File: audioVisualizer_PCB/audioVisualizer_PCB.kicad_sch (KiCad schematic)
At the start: 39 parts, among them J1 USB_C_16P, J2 SWD_DEBUG, J3 SPI_LED_MATRIX, U1 AMS1117-3.3, U7 STM32F401CCUx, Y1 ASE-25MHz

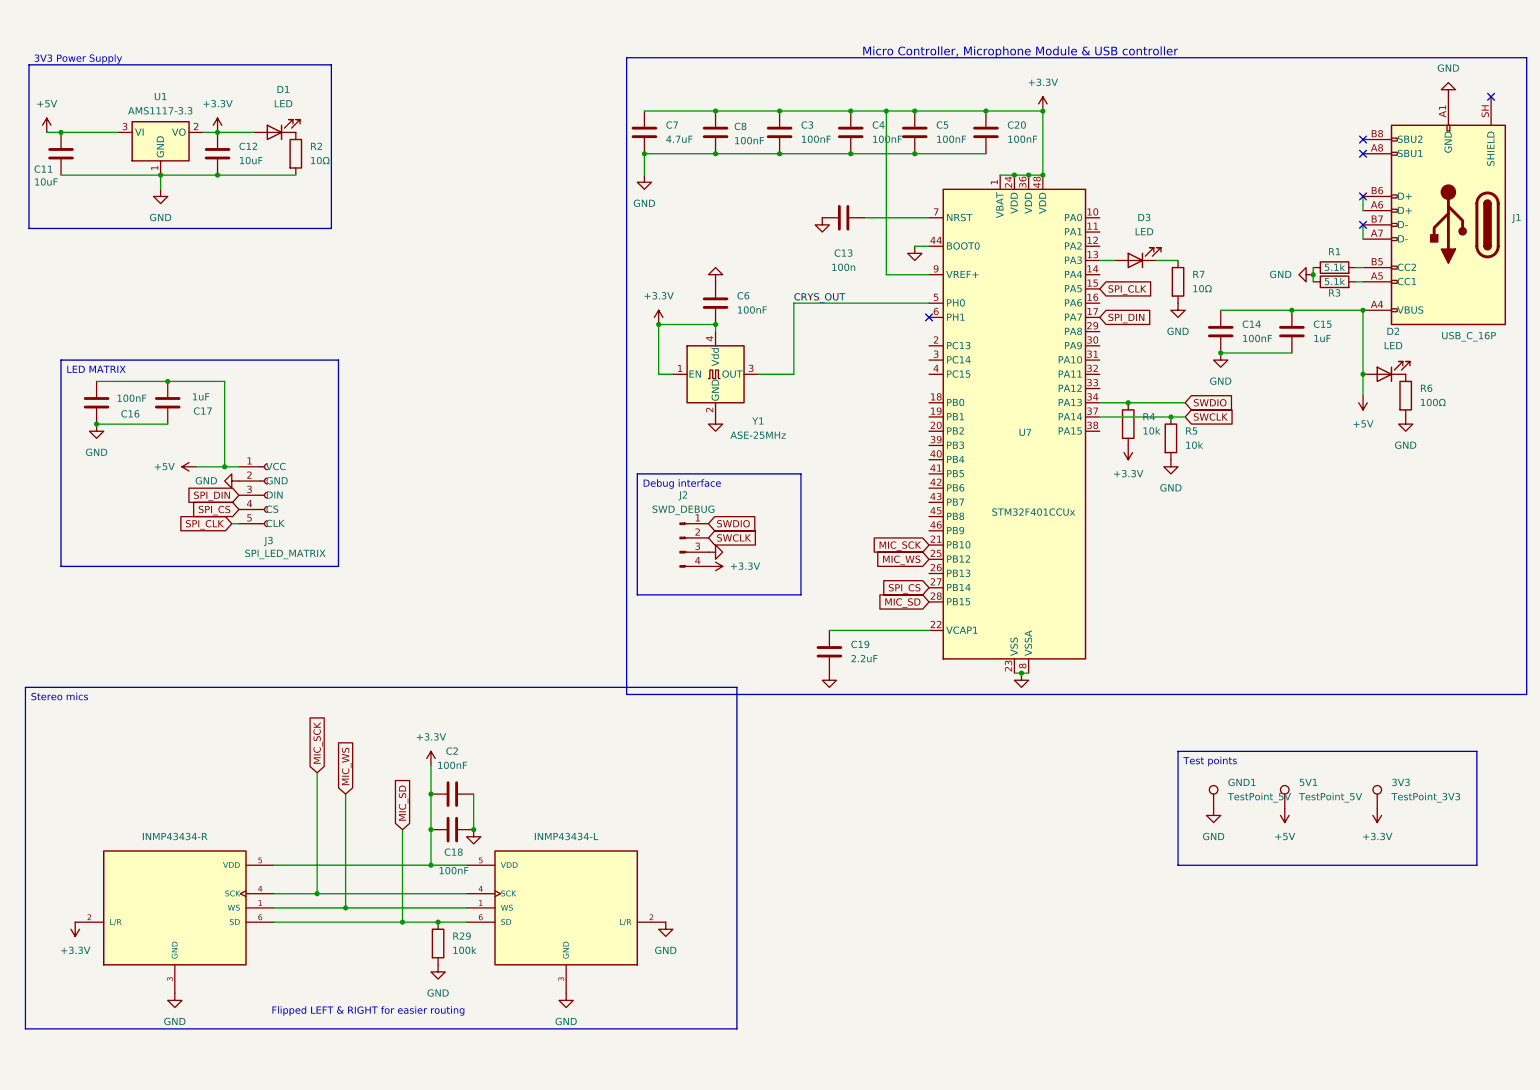
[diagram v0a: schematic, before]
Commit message: update afer review; power fixed?
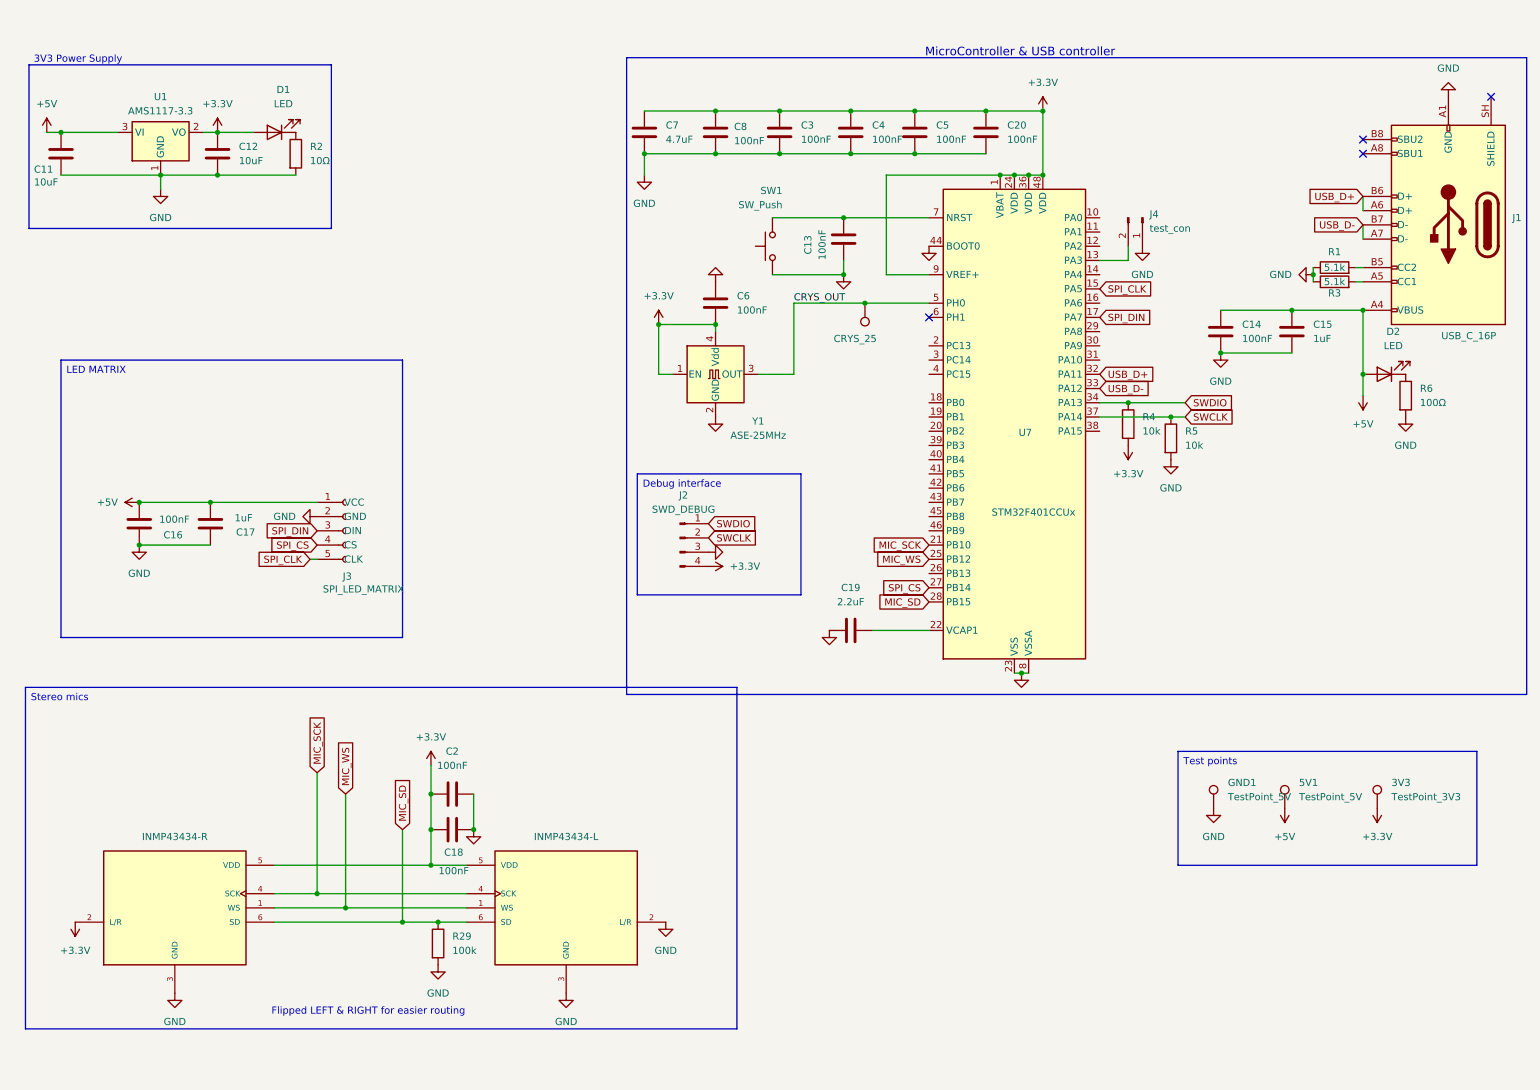
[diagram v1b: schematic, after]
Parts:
- removed D3: LED, LED_SMD:LED_0805_2012Metric, symbol Device:LED
- removed R7: 10Ω, Resistor_SMD:R_0805_2012Metric, symbol Device:R
- added CRYS_25: CRYS_25, TestPoint:TestPoint_Keystone_5015_Micro_Mini, symbol Connector:TestPoint
- added J4: test_con, Connector_PinHeader_2.54mm:PinHeader_1x02_P2.54mm_Vertical, symbol Connector:Conn_01x02_Pin
- added SW1: SW_Push, symbol Switch:SW_Push
- 3V3, 5V1, GND1: footprint TestPoint:TestPoint_Pad_1.0x1.0mm -> TestPoint:TestPoint_Keystone_5015_Micro_Mini
- C13: value 100n -> 100nF
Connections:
- net CRYS_OUT: now also CRYS_25.1
- net GND: now also J4.1 (Pin_1), SW1.1
- net at U7.13 (PA3): now also J4.2 (Pin_2)
- net USB_D+: now reaches U7.32 (PA11)
- net USB_D+: now also J1.A6 (D+), J1.B6 (D+)
- net USB_D-: now reaches U7.33 (PA12)
- net USB_D-: now also J1.A7 (D-), J1.B7 (D-)
- net at C13.1, U7.7 (NRST): now also SW1.2
- no-connect marks 6 -> 4
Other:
- note added: "MicroController & USB controller"
- note removed: "Micro Controller, Microphone Module & USB controller"
- moved on the sheet: C13, C16, C17, C19, J3

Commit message: update
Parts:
- removed J4: test_con, Connector_PinHeader_2.54mm:PinHeader_1x02_P2.54mm_Vertical, symbol Connector:Conn_01x02_Pin
- removed U7: STM32F401CCUx, Package_DFN_QFN:QFN-48-1EP_7x7mm_P0.5mm_EP5.6x5.6mm, symbol MCU_ST_STM32F4:STM32F401CCUx
- added R7: 10kΩ, Resistor_SMD:R_0805_2012Metric, symbol Device:R
- added U2: STM32F401RETx, Package_QFP:LQFP-64_10x10mm_P0.5mm, symbol MCU_ST_STM32F4:STM32F401RETx
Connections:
- net +3.3V: now also R7.1, U2.1 (VBAT), U2.19 (VDD), U2.32 (VDD), U2.48 (VDD), U2.64 (VDD)
- net CRYS_OUT: now also U2.5 (PH0)
- net GND: now also U2.12 (VSSA), U2.18 (VSS), U2.31 (VSS), U2.47 (VSS), U2.60 (BOOT0), U2.63 (VSS)
- net MIC_SCK: now also U2.51 (PC10)
- net MIC_SD: now also U2.53 (PC12)
- net MIC_WS: now also U2.50 (PA15)
- net SPI_CLK: now also U2.34 (PB13)
- net SPI_CS: now also U2.35 (PB14)
- net SPI_DIN: now also U2.36 (PB15)
- net SWCLK: now also U2.49 (PA14)
- net SWDIO: now also U2.46 (PA13)
- net at C19.1: now also U2.30 (VCAP1)
- net at C13.1, SW1.2: now also R7.2, U2.7 (NRST)
- no-connect marks 4 -> 3
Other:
- moved on the sheet: C13, C14, C15, C18, C19, C2, D2, J1, R1, R29, R3, R4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

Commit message: new mcu
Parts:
- removed R7: 10kΩ, Resistor_SMD:R_0805_2012Metric, symbol Device:R
- added R8: 10k, Resistor_SMD:R_0805_2012Metric, symbol Device:R_Small
- SW1: footprint (none) -> Button_Switch_SMD:SW_SPST_TS-1088-xR020
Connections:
- net +3.3V: now also R8.1
- net at C13.1, SW1.2, U2.7 (NRST): now also R8.2
- no-connect marks 3 -> 4
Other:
- moved on the sheet: C13, C14, C15, D2, J1, R1, R3, R6, SW1

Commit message: updated workflow and removed production folder
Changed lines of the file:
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@@
 	)
 	(rectangle
+		(start 17.78 139.7)
+		(end 130.81 196.85)
+		(stroke
+			(width 0)
+			(type default)
+		)
+		(fill
+			(type none)
+		)
+	)
+	(rectangle
 		(start 122.555 14.605)
 		(end 283.21 133.35)
@@
 	(text "Flipped LEFT & RIGHT for easier routing"
 		(exclude_from_sim no)
-		(at 76.454 184.912 0)
+		(at 42.418 152.654 0)
 		(effects
 			(font
@@
 		(in_pos_files yes)
 		(dnp no)
-		(fields_autoplaced yes)
 		(property "Reference" "#PWR07"
 			(at 269.24 13.97 0)
@@
 		)
 		(property "Value" "GND"
-			(at 269.24 15.24 0)
+			(at 266.7 17.526 0)
 			(show_name no)
 			(do_not_autoplace no)

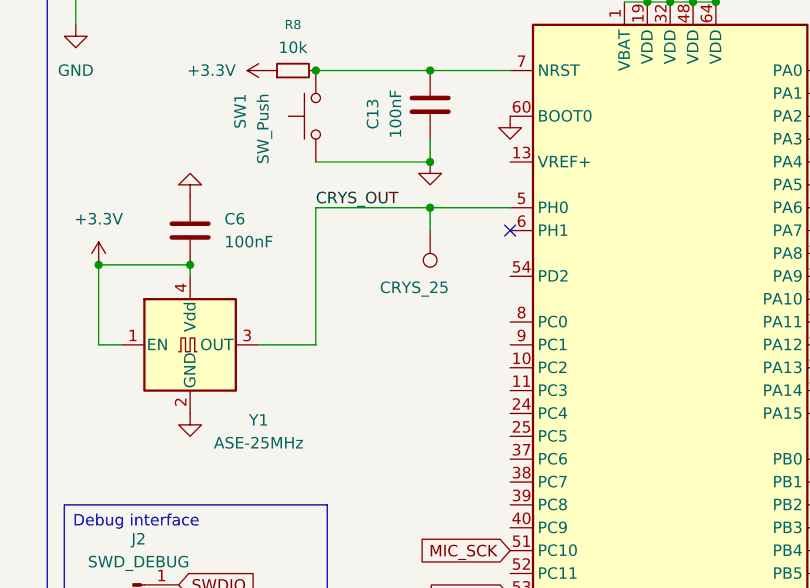
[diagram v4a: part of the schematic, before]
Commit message: add decoup for VREF+ pin
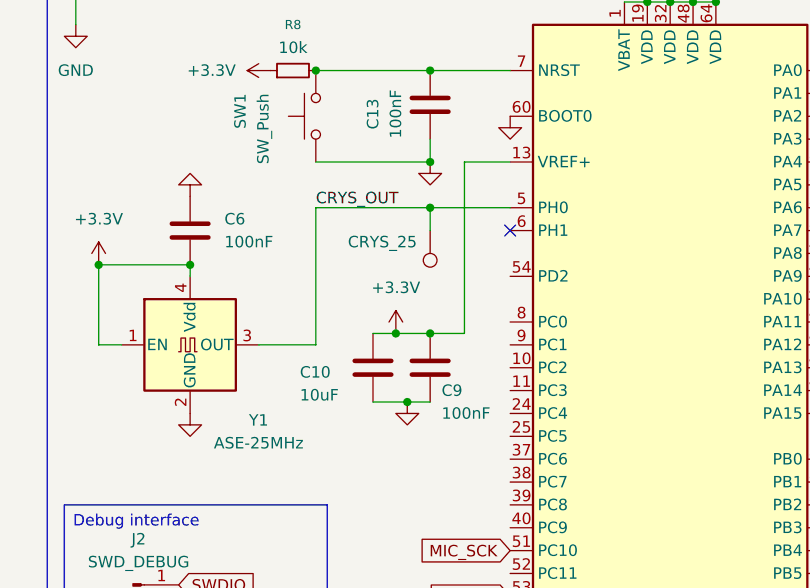
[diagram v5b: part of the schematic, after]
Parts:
- added C10: 10uF, Capacitor_SMD:C_0805_2012Metric, symbol Device:C
- added C9: 100nF, Capacitor_SMD:C_0805_2012Metric, symbol Device:C
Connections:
- net +3.3V: now also U2.13 (VREF+), C10.1, C9.1
- net GND: now also C10.2, C9.2

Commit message: connected the usb, incase it worked
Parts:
- R1, R3: footprint Resistor_SMD:R_0805_2012Metric -> Resistor_SMD:R_1206_3216Metric
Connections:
- net USB_D+: now also U2.45 (PA12)
- net USB_D-: now also U2.44 (PA11)
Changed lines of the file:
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@@
 		)
 	)
+	(global_label "USB_D+"
+		(shape input)
+		(at 209.55 71.12 0)
+		(fields_autoplaced yes)
+		(effects
+			(font
+				(size 1.27 1.27)
+			)
+			(justify left)
+		)
+		(property "Intersheetrefs" "${INTERSHEET_REFS}"
+			(at 220.1552 71.12 0)
+			(hide yes)
+			(show_name no)
+			(do_not_autoplace no)
+			(effects
+				(font
+					(size 1.27 1.27)
+				)
+				(justify left)
+			)
+		)
+	)
 	(global_label "MIC_WS"
 		(shape input)
@@
 		)
 	)
+	(global_label "USB_D-"
+		(shape input)
+		(at 209.55 68.58 0)
+		(fields_autoplaced yes)
+		(effects
+			(font
+				(size 1.27 1.27)
+			)
+			(justify left)
+		)
+		(property "Intersheetrefs" "${INTERSHEET_REFS}"
+			(at 220.1552 68.58 0)
+			(hide yes)
+			(show_name no)
+			(do_not_autoplace no)
+			(effects
+				(font
+					(size 1.27 1.27)
+				)
+				(justify left)
+			)
+		)
+	)
 	(global_label "SWCLK"
 		(shape input)
@@
 			)
 		)
-		(property "Footprint" "Resistor_SMD:R_0805_2012Metric"
+		(property "Footprint" "Resistor_SMD:R_1206_3216Metric"
 			(at 248.92 52.578 90)
 			(hide yes)
@@
 			)
 		)
-		(property "Footprint" "Resistor_SMD:R_0805_2012Metric"
+		(property "Footprint" "Resistor_SMD:R_1206_3216Metric"
 			(at 248.92 55.118 90)
 			(hide yes)
